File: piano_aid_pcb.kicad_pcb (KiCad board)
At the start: 2 copper layers, 44.5 x 61 mm, 38 parts, among them J1 PJ-082BH, J2 796644-3, J3 DIN-5_180degree, J4 Conn_01x06_Female, J5 Micro_SD_Card_Det, J6 Conn_01x07_Female, U1 317030213, U2 6N138, U3 74AHCT1G125W5-7, U4 AZ1117-3.3

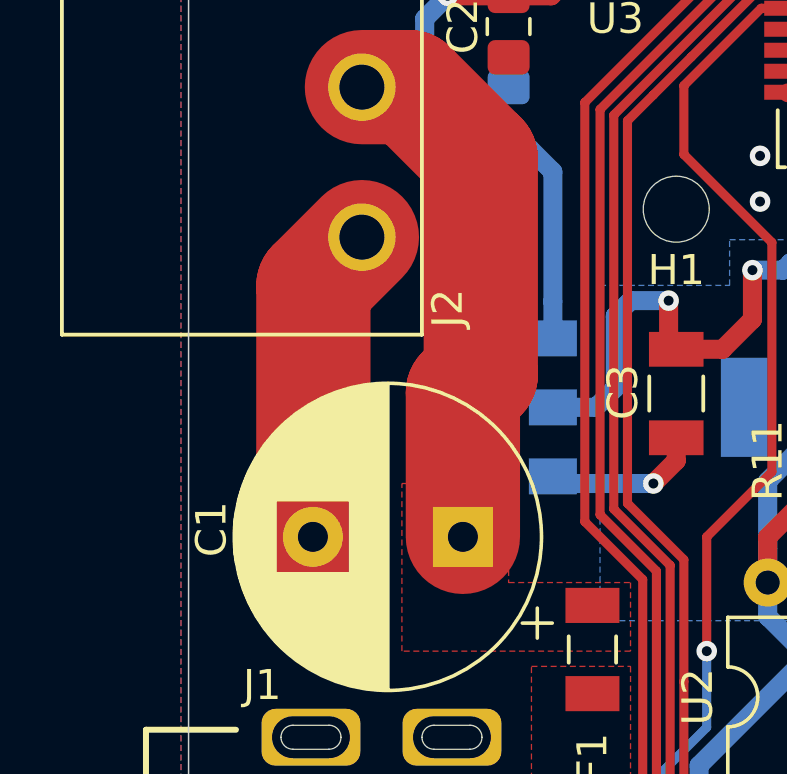
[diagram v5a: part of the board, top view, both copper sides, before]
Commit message: Fixed thermal reliefs
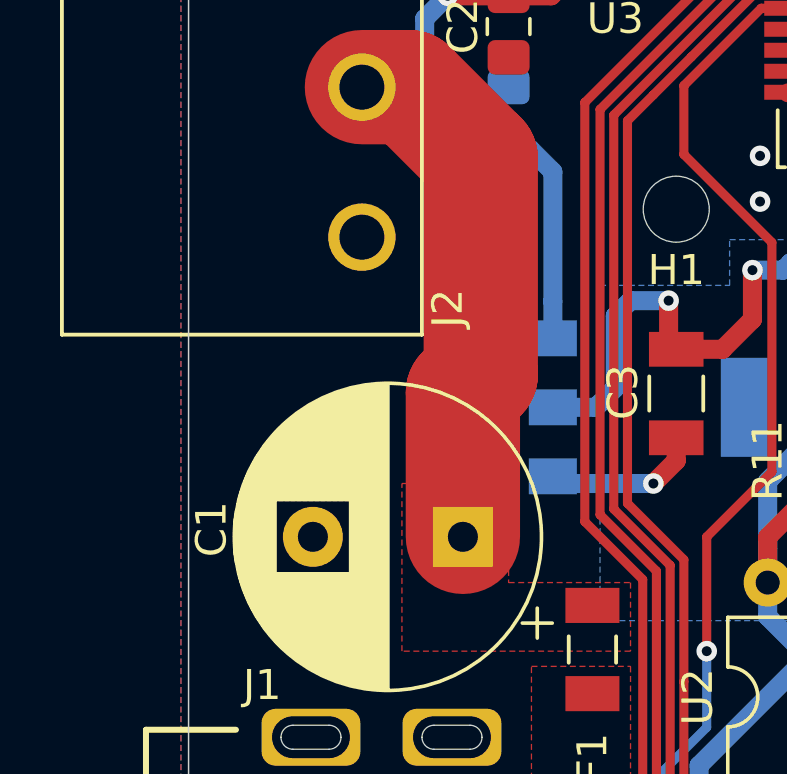
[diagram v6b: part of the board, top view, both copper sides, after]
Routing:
- net GND: track 37.5 -> 26.8 mm
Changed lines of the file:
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@@
     (thickness 1.6)
     (drawings 29)
-    (tracks 315)
+    (tracks 312)
     (zones 0)
     (modules 38)
@@
   (via (at 139.7 85.598) (size 0.6858) (drill 0.3302) (layers F.Cu B.Cu) (net 2))
   (via (at 145.288 81.788) (size 0.6858) (drill 0.3302) (layers F.Cu B.Cu) (net 2))
-  (segment (start 129.794 93.488) (end 129.794 98.298) (width 3.81) (layer F.Cu) (net 1))
   (segment (start 130.390408 92.891592) (end 129.794 93.488) (width 3.81) (layer F.Cu) (net 1))
   (segment (start 130.390408 85.679418) (end 130.390408 92.891592) (width 3.81) (layer F.Cu) (net 1))
@@
   (segment (start 132.7404 80.264) (end 133.5786 79.4258) (width 0.635) (layer F.Cu) (net 1))
   (segment (start 131.318 80.264) (end 132.7404 80.264) (width 0.635) (layer F.Cu) (net 1))
-  (segment (start 124.81 98.314) (end 124.794 98.298) (width 3.81) (layer F.Cu) (net 2))
-  (segment (start 124.81 89.926) (end 124.81 98.314) (width 3.81) (layer F.Cu) (net 2))
-  (segment (start 126.428 88.308) (end 124.81 89.926) (width 3.81) (layer F.Cu) (net 2))
+  (segment (start 129.794 93.488) (end 129.794 98.298) (width 3.81) (layer F.Cu) (net 1))
   (via (at 152.146 74.1803) (size 0.6858) (drill 0.3302) (layers F.Cu B.Cu) (net 2))
   (segment (start 152.1437 74.178) (end 152.146 74.1803) (width 0.635) (layer F.Cu) (net 2))
